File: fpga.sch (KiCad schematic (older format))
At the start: 57 parts, among them P1 JTAG, SW2 BTN0, U10 S25FL216K, U12 TLV70012, U13 TLV70025, U14 TLV70012, U2 EP4CE15E22

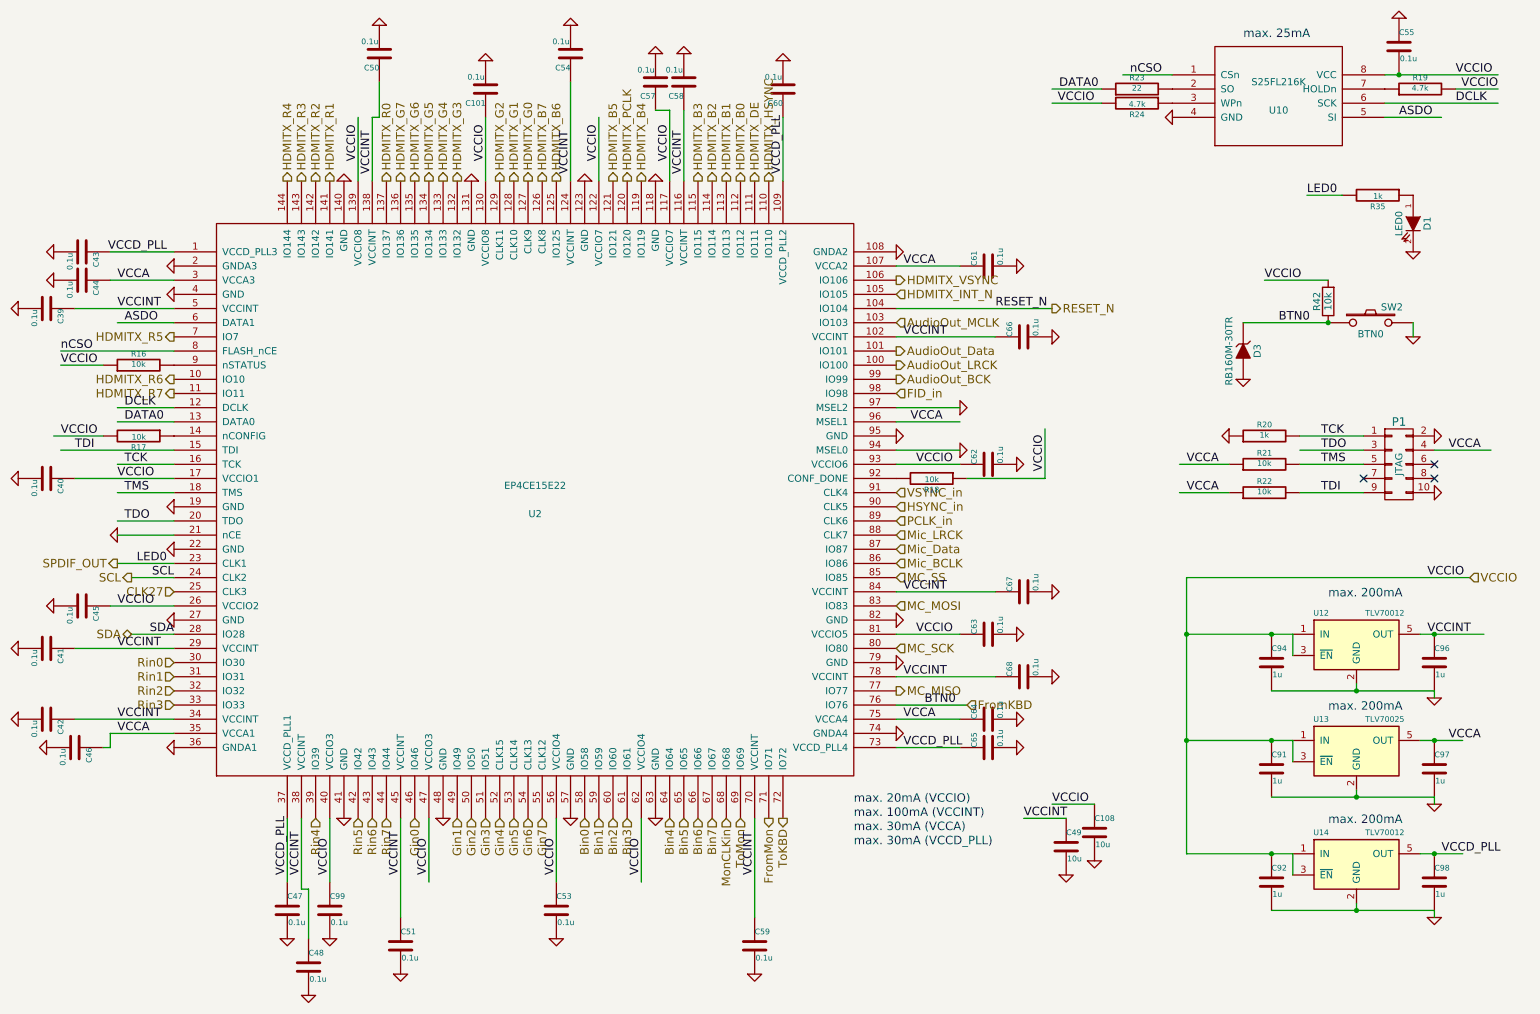
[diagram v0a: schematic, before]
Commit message: update part no
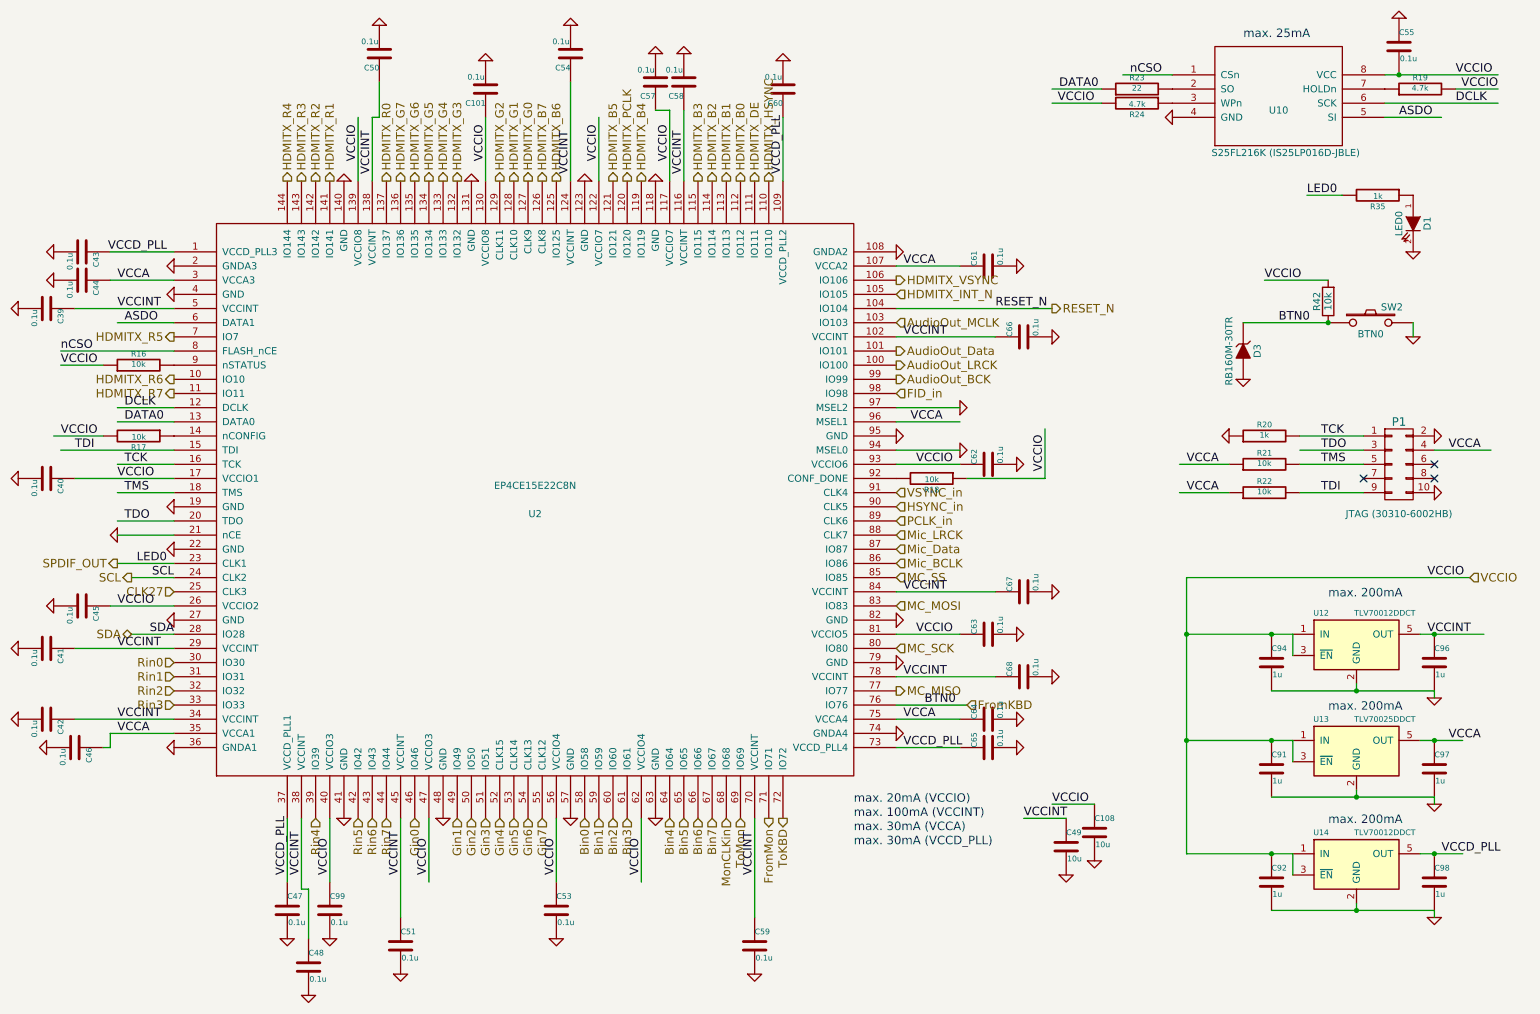
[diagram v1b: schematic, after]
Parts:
- P1: value JTAG -> JTAG (30310-6002HB)
- U10: value S25FL216K -> S25FL216K (IS25LP016D-JBLE)
- U12, U14: value TLV70012 -> TLV70012DDCT
- U13: value TLV70025 -> TLV70025DDCT
- U2: value EP4CE15E22 -> EP4CE15E22C8N
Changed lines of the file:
@@
 P 10350 3850
 F 0 "P1" H 10350 4150 60  0000 C CNN
-F 1 "JTAG" V 10350 3850 50  0000 C CNN
+F 1 "JTAG (30310-6002HB)" H 10350 3500 50  0000 C CNN
 F 2 "Connect:VASCH5x2" H 10350 3850 60  0001 C CNN
 F 3 "" H 10350 3850 60  0000 C CNN
@@
 P 9500 1250
 F 0 "U10" H 9500 1150 50  0000 C CNN
-F 1 "S25FL216K" H 9500 1350 50  0000 C CNN
+F 1 "S25FL216K (IS25LP016D-JBLE)" H 9550 850 50  0000 C CNN
 F 2 "custom_components:SOIC-8_3.9x4.9mm_Pitch1.27mm_Handsoldering" H 9500 1250 50  0001 C CNN
 F 3 "DOCUMENTATION" H 9500 1250 50  0001 C CNN
@@
 AR Path="/54FE3A8C/55035A89" Ref="U14"  Part="1"
 F 0 "U14" H 9800 6850 40  0000 C CNN
-F 1 "TLV70012" H 10250 6850 40  0000 C CNN
+F 1 "TLV70012DDCT" H 10250 6850 40  0000 C CNN
 F 2 "custom_components:SOT-23-5_Handsoldering" H 10050 6750 35  0001 C CIN
 F 3 "" H 10050 6650 60  0000 C CNN
@@
 AR Path="/54FE3A8C/55035DBA" Ref="U13"  Part="1"
 F 0 "U13" H 9800 6050 40  0000 C CNN
-F 1 "TLV70025" H 10250 6050 40  0000 C CNN
+F 1 "TLV70025DDCT" H 10250 6050 40  0000 C CNN
 F 2 "custom_components:SOT-23-5_Handsoldering" H 10050 5950 35  0001 C CIN
 F 3 "" H 10050 5850 60  0000 C CNN
@@
 AR Path="/54FE3A8C/55089296" Ref="U12"  Part="1"
 F 0 "U12" H 9800 5300 40  0000 C CNN
-F 1 "TLV70012" H 10250 5300 40  0000 C CNN
+F 1 "TLV70012DDCT" H 10250 5300 40  0000 C CNN
 F 2 "custom_components:SOT-23-5_Handsoldering" H 10050 5200 35  0001 C CIN
 F 3 "" H 10050 5100 60  0000 C CNN
@@
 P 4250 4100
 F 0 "U2" H 4250 4000 50  0000 C CNN
-F 1 "EP4CE15E22" H 4250 4200 50  0000 C CNN
+F 1 "EP4CE15E22C8N" H 4250 4200 50  0000 C CNN
 F 2 "custom_components:TQFP-144_thermal" H 4250 4100 50  0001 C CNN
 F 3 "DOCUMENTATION" H 4250 4100 50  0001 C CNN

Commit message: update tracks
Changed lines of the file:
@@
 Text HLabel 6800 4550 2    60   Input ~ 0
 Mic_BCLK
+Text HLabel 6800 4450 2    60   Input ~ 0
+Mic_LRCK
 Text HLabel 6800 4350 2    60   Input ~ 0
-Mic_LRCK
-Text HLabel 6800 4450 2    60   Input ~ 0
 Mic_Data
 Text HLabel 1300 4550 0    60   Output ~ 0

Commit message: add more tracks
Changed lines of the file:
@@
 Text HLabel 6800 4650 2    60   Input ~ 0
 MC_SS
+Text HLabel 6800 5450 2    60   Input ~ 0
+MC_MOSI
+Text HLabel 6800 5150 2    60   Output ~ 0
+MC_MISO
 Text HLabel 6800 4850 2    60   Input ~ 0
-MC_MOSI
-Text HLabel 6800 5450 2    60   Output ~ 0
-MC_MISO
-Text HLabel 6800 5150 2    60   Input ~ 0
 MC_SCK
 Text HLabel 6800 2850 2    60   Input ~ 0

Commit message: rearrange FPGA pins
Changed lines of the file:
@@
 	-1   0    0    1
 $EndComp
-Text HLabel 1400 5050 0    60   BiDi ~ 0
+Text HLabel 1400 5350 0    60   BiDi ~ 0
 SDA
-Text HLabel 1400 4650 0    60   Output ~ 0
-SCL
-Text HLabel 1700 5250 0    60   Input ~ 0
+Text HLabel 1700 4650 0    60   Input ~ 0
 Rin0
-Text HLabel 1700 5350 0    60   Input ~ 0
+Text HLabel 1700 4750 0    60   Input ~ 0
 Rin1
-Text HLabel 1700 5450 0    60   Input ~ 0
+Text HLabel 1700 5050 0    60   Input ~ 0
 Rin2
 Text HLabel 1700 5550 0    60   Input ~ 0
@@
 Text HLabel 6800 4050 2    60   Input ~ 0
 VSYNC_in
-Text HLabel 6800 3350 2    60   Input ~ 0
-FID_in
-Text HLabel 7900 2750 2    60   Output ~ 0
+Text HLabel 7900 5550 2    60   Output ~ 0
 RESET_N
-Text HLabel 6800 2650 2    60   Input ~ 0
-HDMITX_INT_N
+Text HLabel 6800 3050 2    60   Output ~ 0
+HDMITX_VSYNC
+Text HLabel 6800 2850 2    60   Output ~ 0
+HDMITX_HSYNC
+Text HLabel 6800 2750 2    60   Output ~ 0
+HDMITX_DE
+Text HLabel 6800 2650 2    60   Output ~ 0
+HDMITX_B0
 Text HLabel 6800 2550 2    60   Output ~ 0
-HDMITX_VSYNC
+HDMITX_B1
 Text HLabel 5900 1850 1    60   Output ~ 0
-HDMITX_HSYNC
+HDMITX_B2
 Text HLabel 5800 1850 1    60   Output ~ 0
-HDMITX_DE
-Text HLabel 5700 1850 1    60   Output ~ 0
-HDMITX_B0
-Text HLabel 5600 1850 1    60   Output ~ 0
-HDMITX_B1
+HDMITX_B3
 Text HLabel 5500 1850 1    60   Output ~ 0
-HDMITX_B2
+HDMITX_B5
 Text HLabel 5400 1850 1    60   Output ~ 0
-HDMITX_B3
+HDMITX_B6
 Text HLabel 5000 1850 1    60   Output ~ 0
-HDMITX_B4
-Text HLabel 4800 1850 1    60   Output ~ 0
-HDMITX_B5
-Text HLabel 4400 1850 1    60   Output ~ 0
-HDMITX_B6
-Text HLabel 4300 1850 1    60   Output ~ 0
 HDMITX_B7
 Text HLabel 4900 1850 1    60   Output ~ 0
-HDMITX_PCLK
-Text HLabel 4200 1850 1    60   Output ~ 0
 HDMITX_G0
-Text HLabel 4100 1850 1    60   Output ~ 0
+Text HLabel 4800 1850 1    60   Output ~ 0
 HDMITX_G1
-Text HLabel 4000 1850 1    60   Output ~ 0
+Text HLabel 4400 1850 1    60   Output ~ 0
 HDMITX_G2
 Text HLabel 3700 1850 1    60   Output ~ 0
@@
 	-1   0    0    1
 $EndComp
-Text Label 1650 4550 2    60   ~ 0
+Text Label 1650 5250 2    60   ~ 0
 LED0
 $Comp
@@
 Text HLabel 10850 4650 2    60   Input ~ 0
 VCCIO
-Text Label 1700 5050 2    60   ~ 0
+Text Label 1700 5350 2    60   ~ 0
 SDA
-Text Label 1700 4650 2    60   ~ 0
-SCL
 $Comp
 L ossc_board-rescue:C-RESCUE-ossc_board C55
@@
 	-1   0    0    1
 $EndComp
-Text HLabel 1700 4750 0    60   Input ~ 0
+Text HLabel 1700 4550 0    60   Input ~ 0
 CLK27
 $Comp
@@
 	8850 4650 10850 4650
 Wire Wire Line
-	6800 2750 7900 2750
+	6800 5550 7900 5550
 Connection ~ 10350 1100
 Wire Wire Line
@@
 Text Label 9400 2550 0    60   ~ 0
 VCCIO
-Text Label 7000 5550 0    60   ~ 0
+Text Label 4100 1850 1    60   ~ 0
 BTN0
 Wire Wire Line
-	1300 4550 1700 4550
+	1300 5250 1700 5250
 Connection ~ 8850 5050
 Text Notes 9250 850  0    60   ~ 0
@@
 Text Notes 6500 6550 0    60   ~ 0
 max. 30mA (VCCD_PLL)
-Text Label 7500 2750 0    60   ~ 0
+Text Label 7500 5550 0    60   ~ 0
 RESET_N
 $Comp
@@
 Wire Wire Line
 	8850 5050 8850 5800
-Wire Wire Line
-	1700 4650 1400 4650
 $Comp
 L ossc_board-rescue:GND-RESCUE-ossc_board #PWR0209
@@
 Connection ~ 9850 2850
 Wire Wire Line
-	5000 6350 5000 6800
-Wire Wire Line
-	4400 6350 4400 6800
-Wire Wire Line
-	5200 1350 5200 1850
-Wire Wire Line
-	3500 6350 3500 6800
-Wire Wire Line
-	3300 6350 3300 7050
-Wire Wire Line
-	5300 1350 5300 1850
-Wire Wire Line
-	2800 6350 2800 6800
-Wire Wire Line
-	2600 6350 2600 6850
-Wire Wire Line
-	2500 6800 2500 6350
-Wire Wire Line
-	3000 1850 3000 1400
-Wire Wire Line
-	3100 1850 3100 1400
-Wire Wire Line
-	3900 1850 3900 1400
-Wire Wire Line
-	4500 1150 4500 1850
-Wire Wire Line
-	4700 1850 4700 1400
-Wire Wire Line
-	5800 6350 5800 7050
-Wire Wire Line
-	6000 1850 6000 1400
-$Comp
-L ossc_board-rescue:EP4CE15E22 U2
-U 1 1 54FE3D0C
-P 4250 4100
-F 0 "U2" H 4250 4000 50  0000 C CNN
-F 1 "EP4CE15E22C8N" H 4250 4200 50  0000 C CNN
-F 2 "custom_components:TQFP-144_thermal" H 4250 4100 50  0001 C CNN
-F 3 "DOCUMENTATION" H 4250 4100 50  0001 C CNN
-	1    4250 4100
-	1    0    0    -1
-$EndComp
-Wire Wire Line
-	1700 5050 1400 5050
+	1700 5350 1400 5350
 Text HLabel 5600 6350 3    60   Input ~ 0
 MonCLKin
@@
 Text HLabel 6800 4850 2    60   Input ~ 0
 MC_SCK
-Text HLabel 6800 2850 2    60   Input ~ 0
-AudioOut_MCLK
+Text HLabel 6800 3350 2    60   Output ~ 0
+AudioOut_BCK
 Text HLabel 6800 3250 2    60   Output ~ 0
-AudioOut_BCK
+AudioOut_LRCK
 Text HLabel 6800 3150 2    60   Output ~ 0
-AudioOut_LRCK
-Text HLabel 6800 3050 2    60   Output ~ 0
 AudioOut_Data
-Text HLabel 6800 4550 2    60   Input ~ 0
-Mic_BCLK
-Text HLabel 6800 4450 2    60   Input ~ 0
-Mic_LRCK
-Text HLabel 6800 4350 2    60   Input ~ 0
-Mic_Data
-Text HLabel 1300 4550 0    60   Output ~ 0
+Text HLabel 1300 5250 0    60   Output ~ 0
 SPDIF_OUT
-Text HLabel 7300 5550 2    60   Input ~ 0
+Text HLabel 4100 1500 1    60   Input ~ 0
 FromKBD
 Text HLabel 6000 6350 3    60   Output ~ 0
 ToKBD
-Wire Wire Line
-	6800 5550 7300 5550
 $Comp
 L ossc_board-rescue:ZENER D3
@@
 Wire Wire Line
 	8850 5050 9450 5050
+Text HLabel 4300 1850 1    60   Input ~ 0
+FID_in
+Text HLabel 4200 1850 1    60   Input ~ 0
+AudioOut_MCLK
+Text HLabel 4000 1850 1    60   Input ~ 0
+HDMITX_INT_N
+Text HLabel 5700 1850 1    60   Output ~ 0
+HDMITX_B4
+Text HLabel 5600 1850 1    60   Output ~ 0
+HDMITX_PCLK
+Text HLabel 6800 4350 2    60   Input ~ 0
+Mic_Data
+Text HLabel 6800 4450 2    60   Input ~ 0
+Mic_LRCK
+Text HLabel 6800 4550 2    60   Input ~ 0
+Mic_BCLK
+Wire Wire Line
+	5000 6350 5000 6800
+Wire Wire Line
+	4400 6350 4400 6800
+Wire Wire Line
+	5200 1350 5200 1850
+Wire Wire Line
+	3500 6350 3500 6800
+Wire Wire Line
+	3300 6350 3300 7050
+Wire Wire Line
+	5300 1350 5300 1850
+Wire Wire Line
+	2800 6350 2800 6800
+Wire Wire Line
+	2600 6350 2600 6850
+Wire Wire Line
+	2500 6800 2500 6350
+Wire Wire Line
+	3000 1850 3000 1400
+Wire Wire Line
+	3100 1850 3100 1400
+Wire Wire Line
+	3900 1850 3900 1400
+Wire Wire Line
+	4100 1500 4100 1850
+Wire Wire Line
+	4500 1150 4500 1850
+Wire Wire Line
+	4700 1850 4700 1400
+Wire Wire Line
+	5800 6350 5800 7050
+Wire Wire Line
+	6000 1850 6000 1400
+$Comp
+L ossc_board-rescue:EP4CE15E22 U2
+U 1 1 54FE3D0C
+P 4250 4100
+F 0 "U2" H 4250 4000 50  0000 C CNN
+F 1 "EP4CE15E22C8N" H 4250 4200 50  0000 C CNN
+F 2 "custom_components:TQFP-144_thermal" H 4250 4100 50  0001 C CNN
+F 3 "DOCUMENTATION" H 4250 4100 50  0001 C CNN
+	1    4250 4100
+	1    0    0    -1
+$EndComp
+Text HLabel 1400 5450 0    60   Output ~ 0
+SCL
+Text Label 1700 5450 2    60   ~ 0
+SCL
+Wire Wire Line
+	1700 5450 1400 5450
 $EndSCHEMATC

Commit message: update values
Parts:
- U13: value TLV70025DDCT -> TLV70025DDCT(TPS79925DDCR)
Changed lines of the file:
@@
 max. 200mA
-$Comp
-L ossc_board-rescue:TLV71209DBV-RESCUE-ossc_board U?
-U 1 1 55035DBA
-P 10050 5850
-AR Path="/55035DBA" Ref="U?"  Part="1"
-AR Path="/54FE3A8C/55035DBA" Ref="U13"  Part="1"
-F 0 "U13" H 9800 6050 40  0000 C CNN
-F 1 "TLV70025DDCT" H 10250 6050 40  0000 C CNN
-F 2 "custom_components:SOT-23-5_Handsoldering" H 10050 5950 35  0001 C CIN
-F 3 "" H 10050 5850 60  0000 C CNN
-	1    10050 5850
-	1    0    0    -1
-$EndComp
 $Comp
 L ossc_board-rescue:C-RESCUE-ossc_board C91
@@
 Wire Wire Line
 	9600 6600 9600 6750
-Connection ~ 9450 5800
 Connection ~ 10600 5800
 Wire Wire Line
 	10600 6200 10600 6250
-Connection ~ 10050 6200
-Wire Wire Line
-	10050 6150 10050 6200
-Wire Wire Line
-	9450 6200 10050 6200
 Wire Wire Line
 	8850 5800 9450 5800
-Wire Wire Line
-	10500 5800 10600 5800
-Wire Wire Line
-	9600 5800 9600 5950
 Connection ~ 10600 5050
 Wire Wire Line
@@
 	10050 7000 10600 7000
 Wire Wire Line
-	9450 5800 9600 5800
-Wire Wire Line
 	10600 5800 10800 5800
-Wire Wire Line
-	10050 6200 10600 6200
 Wire Wire Line
 	10600 5050 10950 5050
@@
 Wire Wire Line
 	1700 5450 1400 5450
+Wire Wire Line
+	10500 5800 10600 5800
+Connection ~ 9450 5800
+Wire Wire Line
+	9450 5800 9600 5800
+Wire Wire Line
+	9600 5800 9600 5950
+Wire Wire Line
+	10050 6200 10600 6200
+Wire Wire Line
+	9450 6200 10050 6200
+Connection ~ 10050 6200
+Wire Wire Line
+	10050 6150 10050 6200
+$Comp
+L ossc_board-rescue:TLV71209DBV-RESCUE-ossc_board U?
+U 1 1 55035DBA
+P 10050 5850
+AR Path="/55035DBA" Ref="U?"  Part="1"
+AR Path="/54FE3A8C/55035DBA" Ref="U13"  Part="1"
+F 0 "U13" H 9800 6050 40  0000 C CNN
+F 1 "TLV70025DDCT(TPS79925DDCR)" H 10400 6050 40  0000 C CNN
+F 2 "custom_components:SOT-23-5_Handsoldering" H 10050 5950 35  0001 C CIN
+F 3 "" H 10050 5850 60  0000 C CNN
+	1    10050 5850
+	1    0    0    -1
+$EndComp
 $EndSCHEMATC
